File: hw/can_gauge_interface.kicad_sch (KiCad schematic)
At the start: 26 parts, among them J3 Power debug, J4 Power debug, J5 SPI debug, J6 I^{2}C debug, J7 CAN debug, U5 MCP48FVB14/MQ, U6 ATA6563-GAQW1, U7 N24C32UDTG

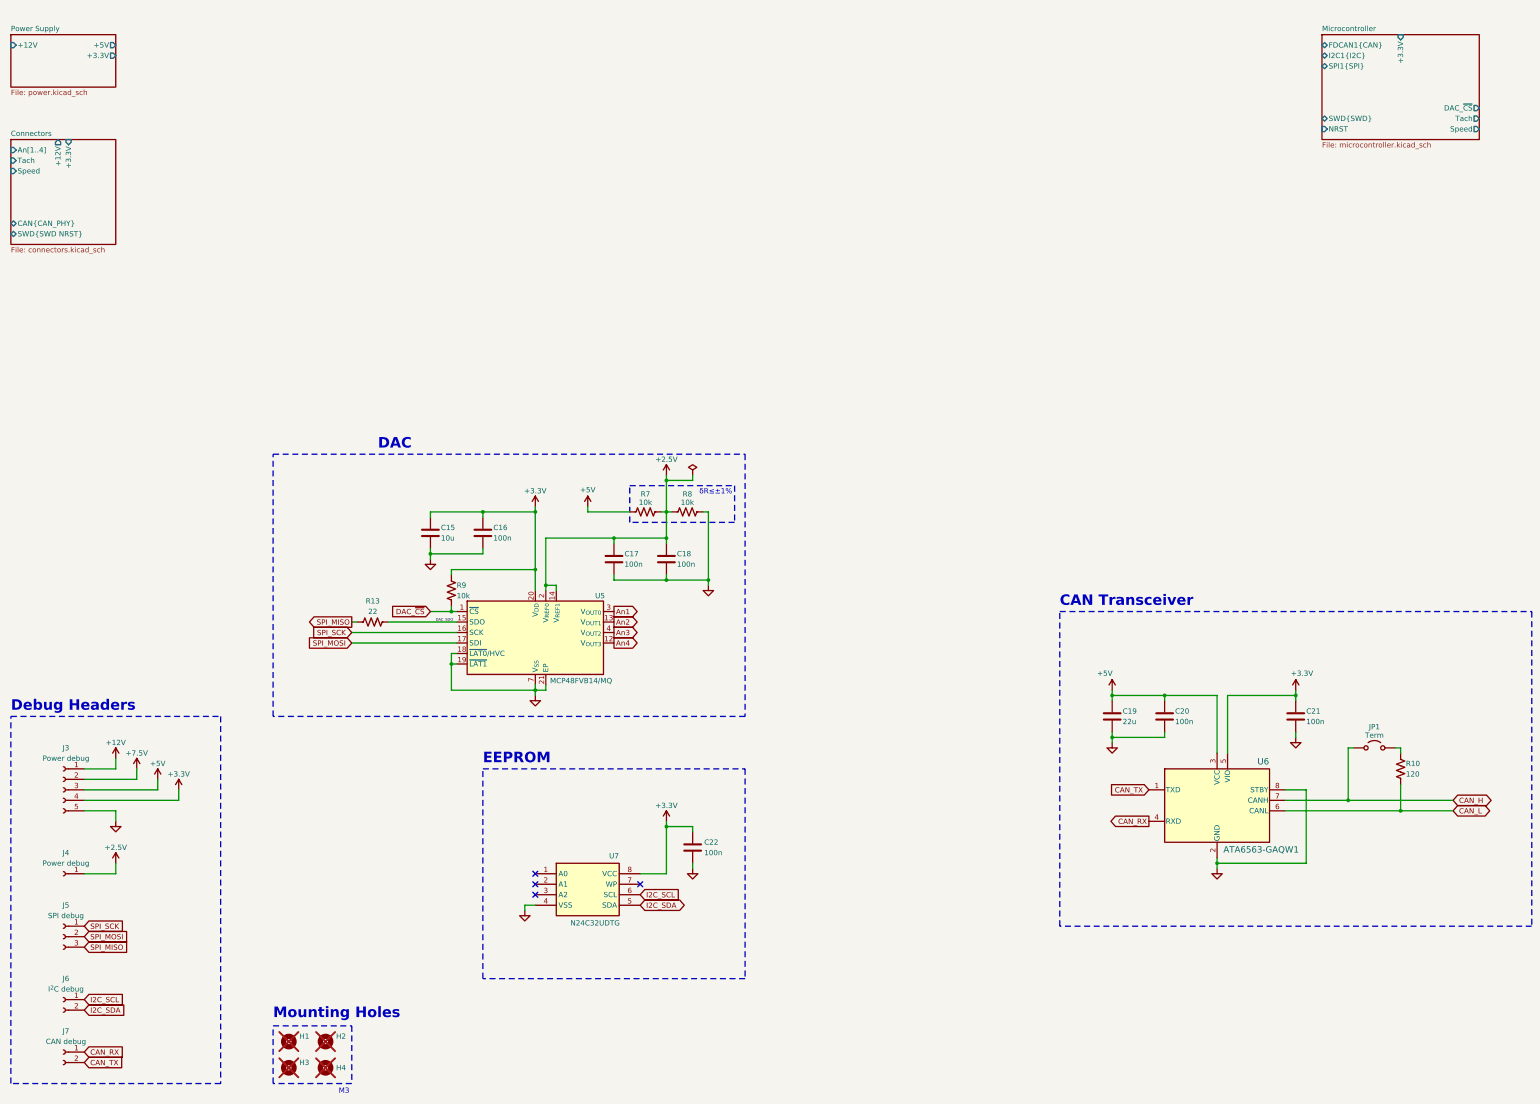
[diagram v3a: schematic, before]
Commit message: hw: dac hierarchical sheet
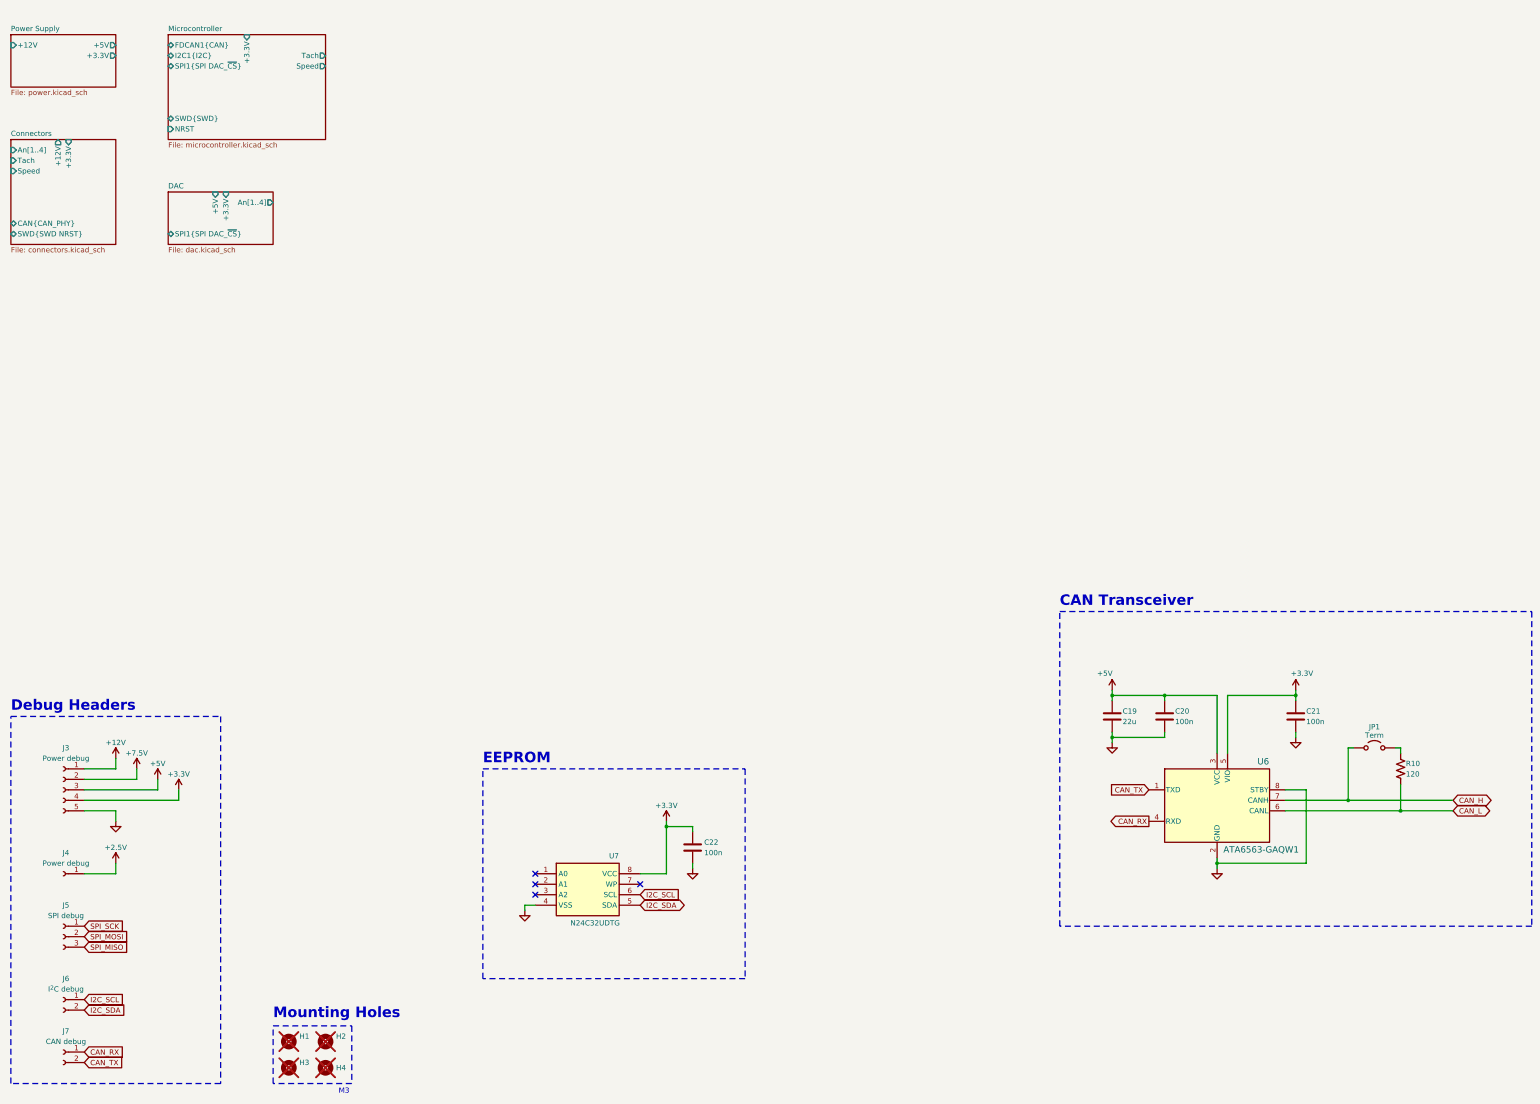
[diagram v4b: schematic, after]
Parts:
- removed C15: 10u, Capacitor_SMD:C_0805_2012Metric, symbol Device:C
- removed C16, C17, C18: 100n, Capacitor_SMD:C_0402_1005Metric, symbol Device:C
- removed R13: 22, Resistor_SMD:R_0603_1608Metric, symbol Device:R_US
- removed R7, R8, R9: 10k, Resistor_SMD:R_0603_1608Metric, symbol Device:R_US
- removed U5: MCP48FVB14/MQ, Package_DFN_QFN:Texas_RGW0020A_VQFN-20-1EP_5x5mm_P0.65mm_EP3.15x3.15mm, symbol symbols:MCP48FVB14/MQ
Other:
- added sheet DAC (dac.kicad_sch)
- sheet Microcontroller ports: added SPI1{SPI DAC_~{CS}}; removed DAC_~{CS}, SPI1{SPI}
- note removed: "DAC"
- note removed: "δR≤±1%"

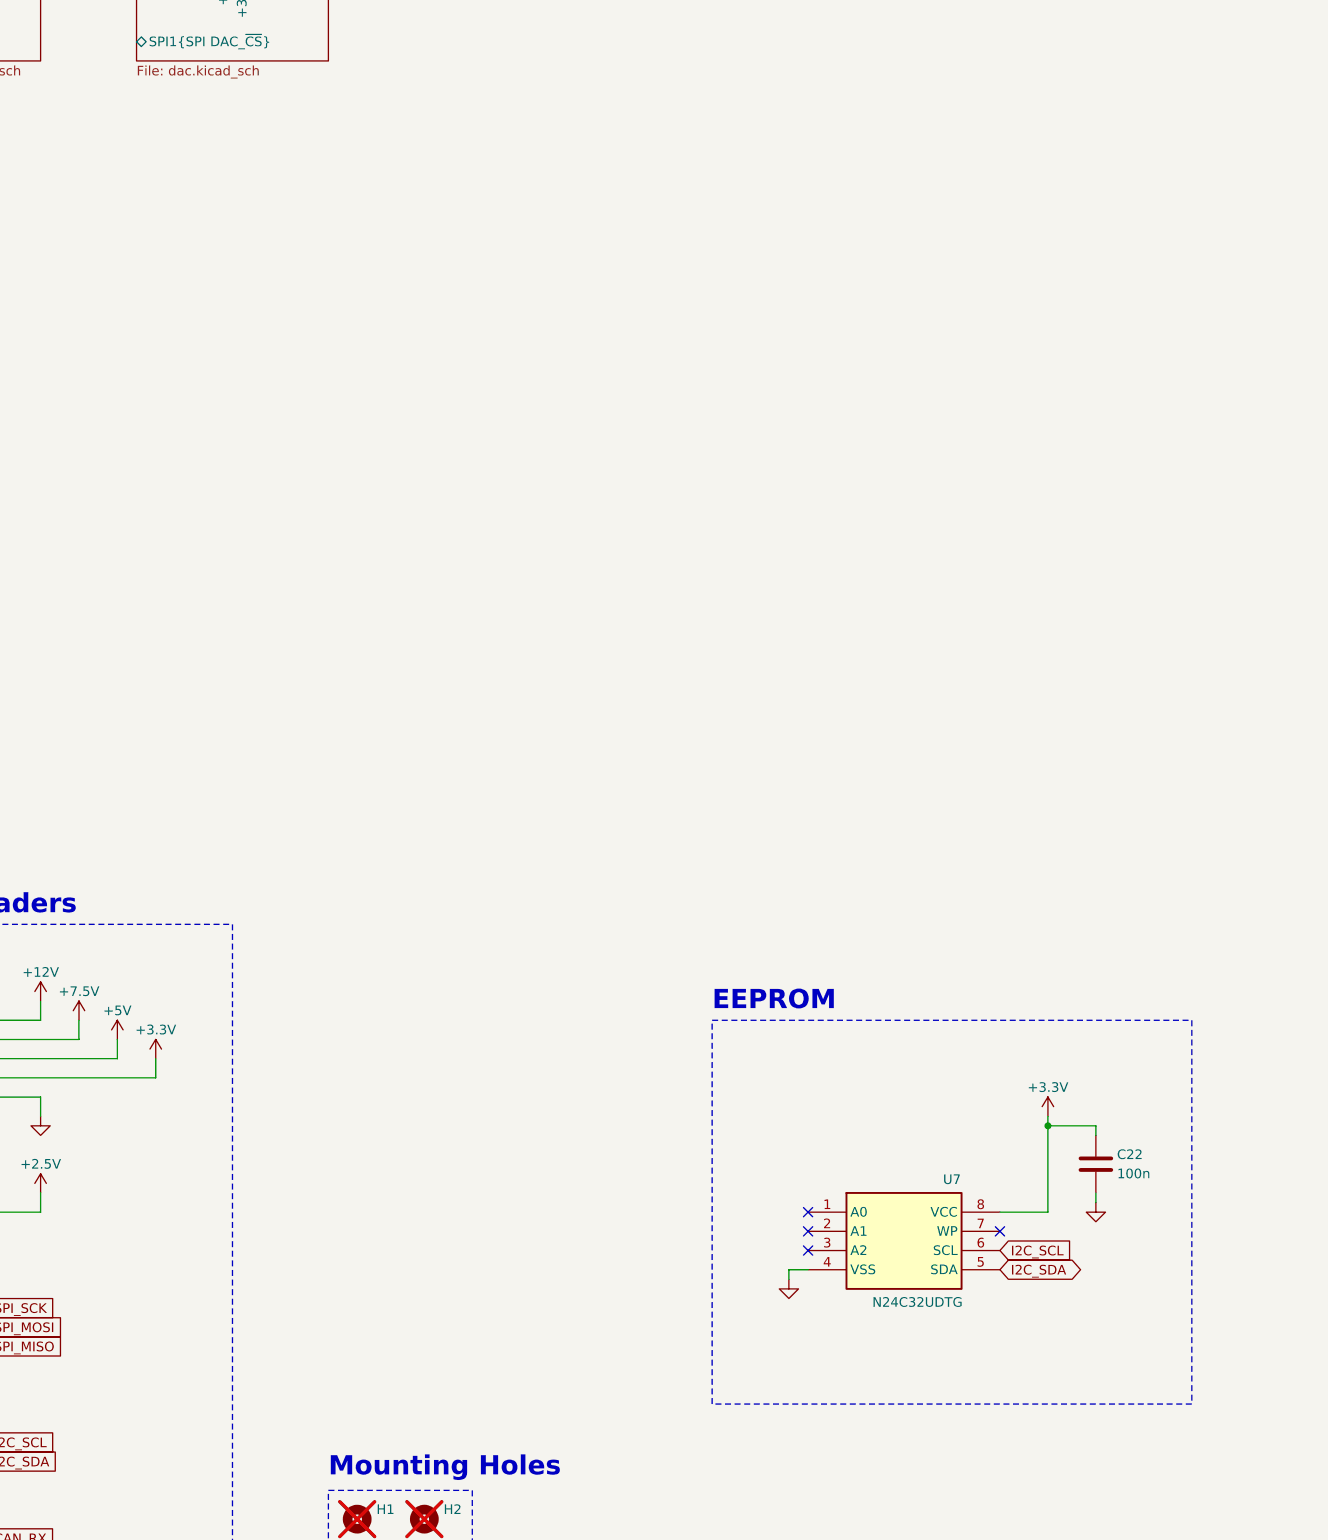
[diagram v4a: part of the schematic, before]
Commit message: hw: eeprom hierarchical sheet
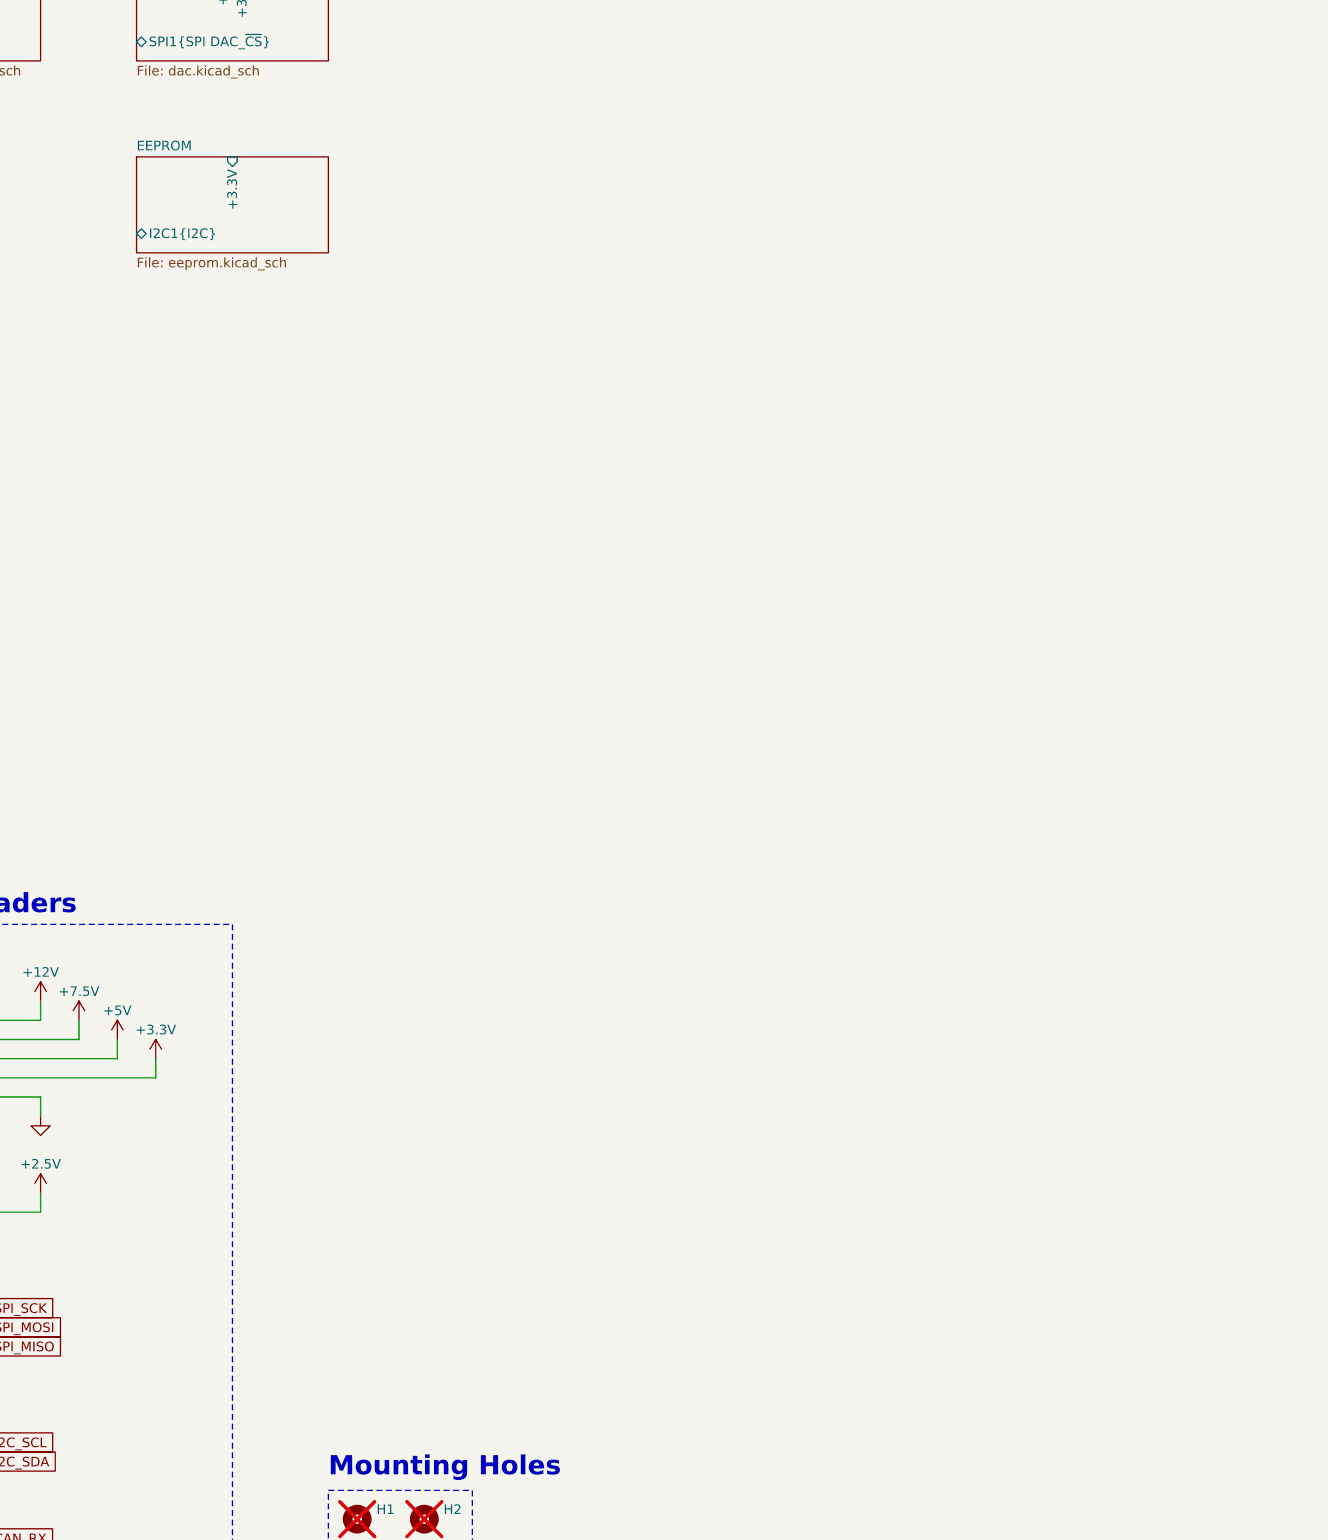
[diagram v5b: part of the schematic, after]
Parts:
- removed C22: 100n, Capacitor_SMD:C_0402_1005Metric, symbol Device:C
- removed U7: N24C32UDTG, footprints:SOP50P312X90-8N, symbol N24C32UDTG:N24C32UDTG
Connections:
- no-connect marks 4 -> 0
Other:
- added sheet EEPROM (eeprom.kicad_sch)
- note removed: "EEPROM"
